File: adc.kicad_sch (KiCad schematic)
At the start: 0 parts

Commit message: Starting draft of ADC multiplexer
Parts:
- added D18: BAT54SW, Package_TO_SOT_SMD:SOT-323_SC-70, symbol Diode:BAT54SW
- added Q11, Q12: PMOS, symbol Simulation_SPICE:PMOS
- added Q13: 2N7002, Package_TO_SOT_SMD:SOT-323_SC-70, symbol Transistor_FET:2N7002
- added R40, R44: R, symbol Device:R
- added R45, R47: 1M, Resistor_SMD:R_0603_1608Metric, symbol Device:R
- added R46: 1k, Resistor_SMD:R_0603_1608Metric, symbol Device:R
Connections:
- new net: Q11.2 (G), Q12.2 (G), Q13.3 (D), R45.2
- new net: Q13.1 (G), R46.2, R47.1
- new net: Q11.1 (D), R40.1
- new net: Q11.3 (S), Q12.3 (S)
- new net +BATT: Q12.1 (D), R45.1
- new net GND: D18.1 (A), Q13.2 (S), R44.1, R47.2
- new net VBATT_ADC: D18.3 (COM), R40.2, R44.2
- new net VBATT_ADC_EN: R46.1
- new net VDD: D18.2 (K)
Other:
- note added: "Can multiplex any of the cell voltages to a single voltage divider and ADC pin This makes it possible to get a really good comparison as long as the ADC is linear"

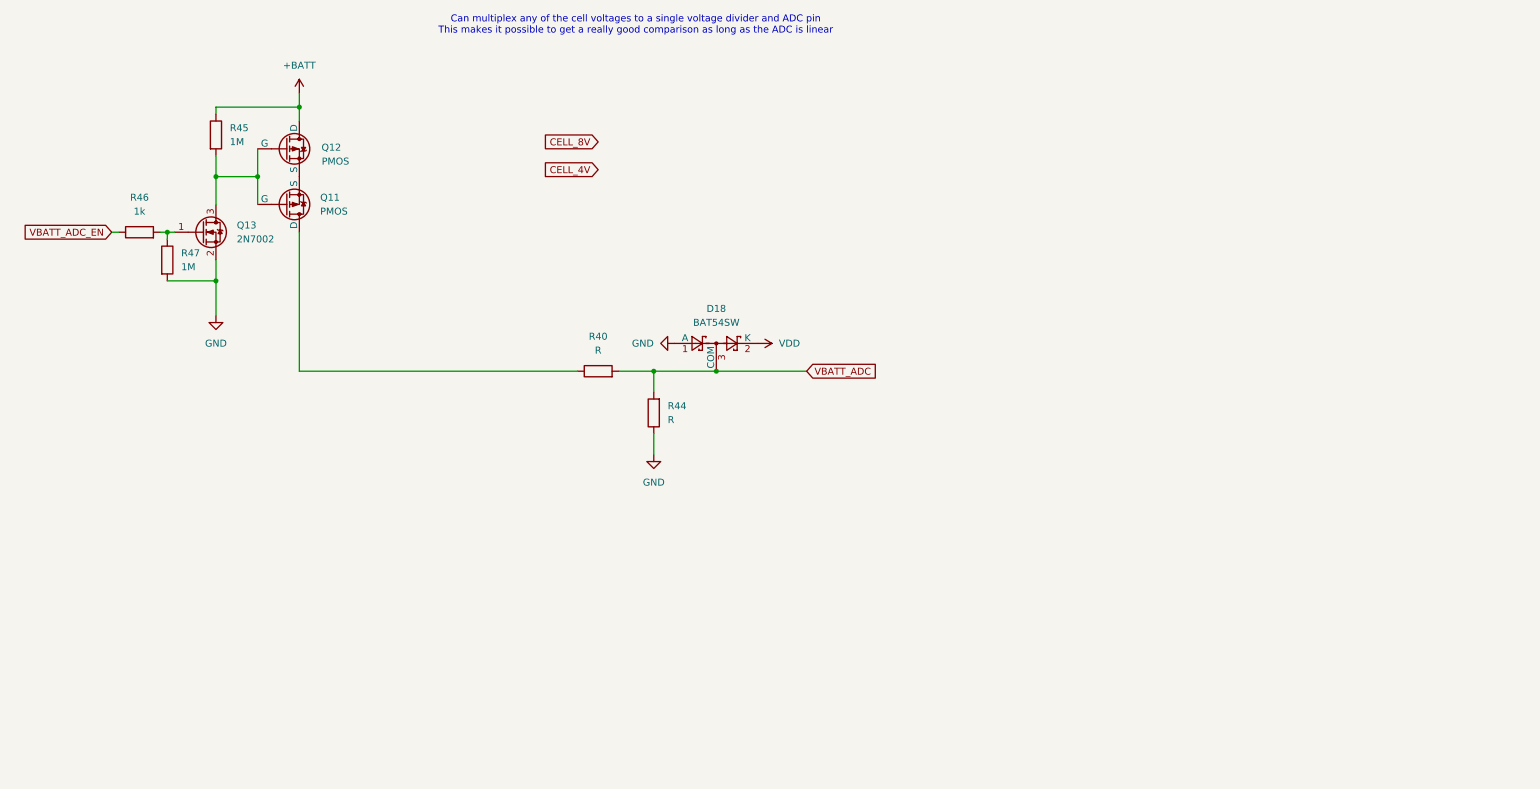
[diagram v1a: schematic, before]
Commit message: Adding ADC multiplexer, protection diodes
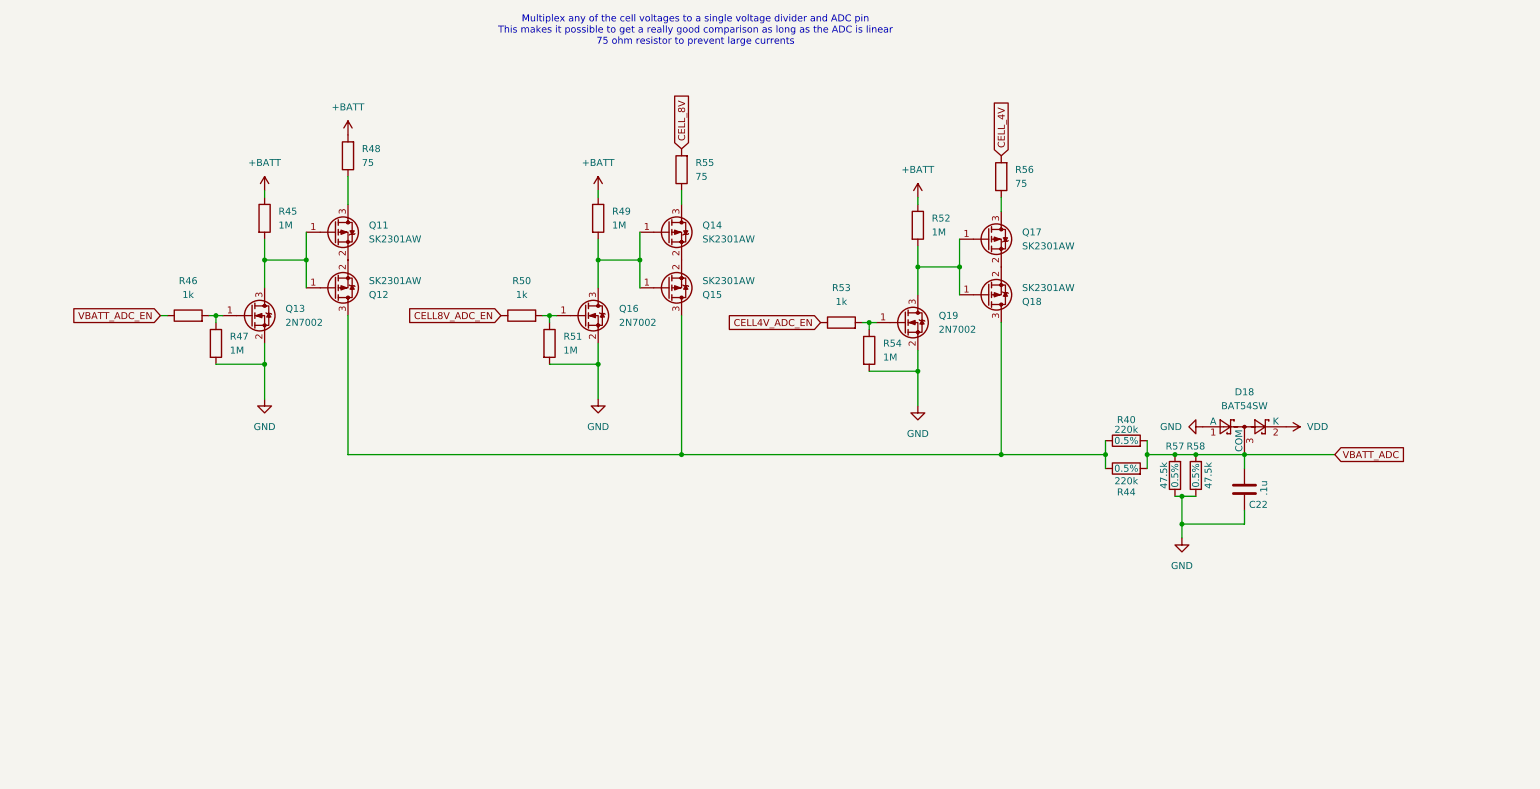
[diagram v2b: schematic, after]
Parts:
- removed Q11, Q12: PMOS, symbol Simulation_SPICE:PMOS
- added C22: .1u, Capacitor_SMD:C_0603_1608Metric, symbol Device:C
- added Q11, Q12, Q14, Q15, Q17, Q18: SK2301AW, Package_TO_SOT_SMD:SOT-323_SC-70, symbol JakeLib:SK2301AW
- added Q16, Q19: 2N7002, Package_TO_SOT_SMD:SOT-323_SC-70, symbol Transistor_FET:2N7002
- added R48, R55, R56: 75, Resistor_SMD:R_0603_1608Metric, symbol Device:R
- added R49, R51, R52, R54: 1M, Resistor_SMD:R_0603_1608Metric, symbol Device:R
- added R50, R53: 1k, Resistor_SMD:R_0603_1608Metric, symbol Device:R
- added R57, R58: 47.5k, Resistor_SMD:R_0402_1005Metric, symbol Device:R
- R40, R44: value R -> 220k; footprint (none) -> Resistor_SMD:R_0402_1005Metric; LCSC_Code (none) -> C851925; Tolerance (none) -> 0.5%
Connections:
- net +BATT: now also R48.2, R49.1, R52.1
- net CELL_4V: now also R56.2
- net CELL_8V: now also R55.2
- net GND: now also C22.2, Q16.2 (S), Q19.2 (S), R51.2, R54.2, R57.1, R58.1; no longer R44.1
- net VBATT_ADC: now also C22.1, R57.2, R58.2
- net at Q13.3 (D), R45.2: now also Q11.1 (G), Q12.1 (G)
- net at R40.1: now also R44.1, Q12.3 (D), Q15.3 (D), Q18.3 (D)
- new net: Q16.1 (G), R50.2, R51.1
- new net: Q11.2 (S), Q12.2 (S)
- new net: Q11.3 (D), R48.1
- new net: Q14.1 (G), Q15.1 (G), Q16.3 (D), R49.2
- new net: Q14.2 (S), Q15.2 (S)
- new net: Q14.3 (D), R55.1
- new net: Q17.1 (G), Q18.1 (G), Q19.3 (D), R52.2
- new net: Q17.3 (D), R56.1
- new net: Q17.2 (S), Q18.2 (S)
- new net: Q19.1 (G), R53.2, R54.1
- new net CELL4V_ADC_EN: R53.1
- new net CELL8V_ADC_EN: R50.1
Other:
- note added: "Multiplex any of the cell voltages to a single voltage divider and ADC pin This makes it possible to get a really good comparison as long as the ADC is linear 75 ohm resistor to prevent large currents"
- note removed: "Can multiplex any of the cell voltages to a single voltage divider and ADC pin This makes it possible to get a really good comparison as long as the ADC is linear"
- moved on the sheet: D18, Q13, R45, R46, R47

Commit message: Taking notes, doing some final adjustments to RC filter values
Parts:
- removed R40, R44: 220k, Resistor_SMD:R_0402_1005Metric, symbol Device:R
- removed R57, R58: 47.5k, Resistor_SMD:R_0402_1005Metric, symbol Device:R
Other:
- note added: "You want ~1/6 ratio so that 12V comes to around 2V. 1.5kohm max total impedance, because you are sampling frequently (Impedance goes to charge ~20pf adc capacitor, so that takes time, limiting sampling rate) (Also, at 80khz sampling rate, you have ~4uA current, to charge the 20pf capacitor, leading to voltage drop)"

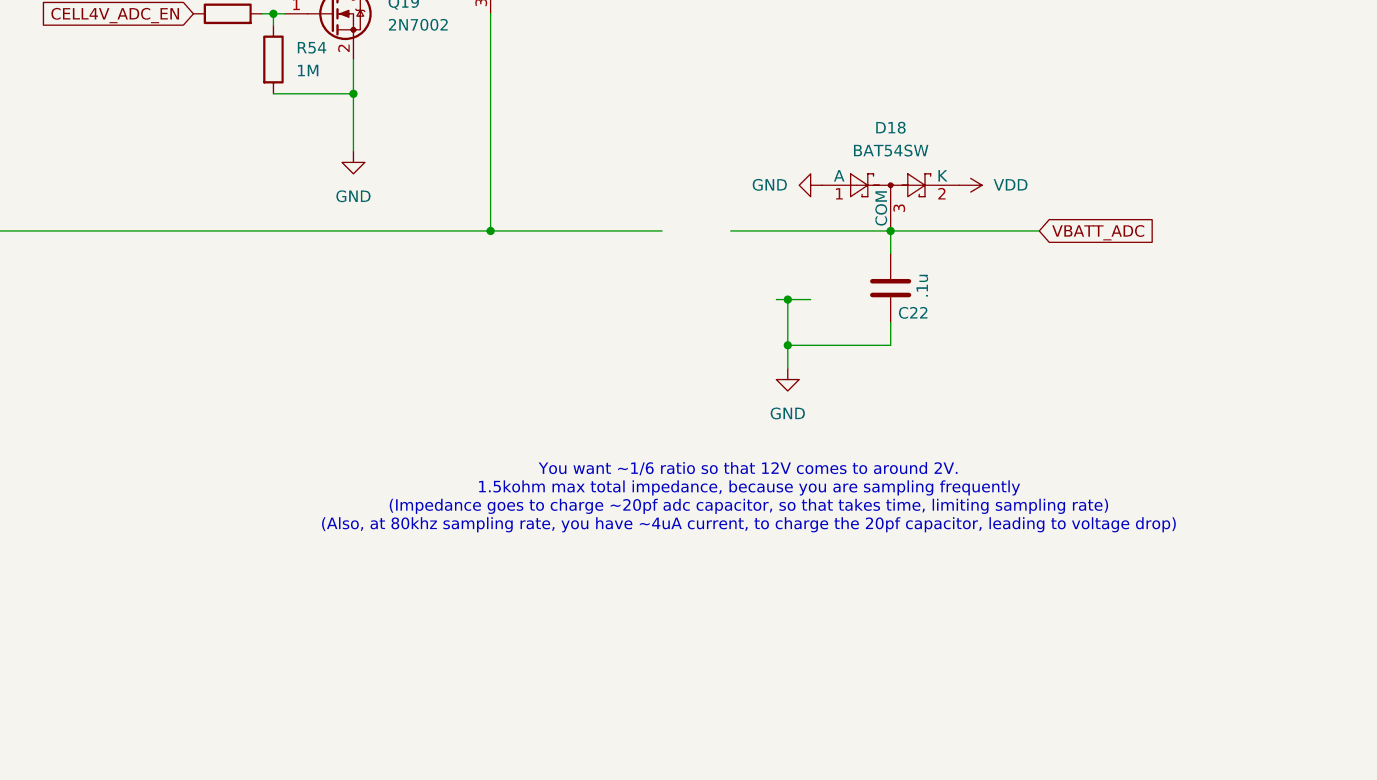
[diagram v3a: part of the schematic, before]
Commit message: L6388E mosfet drivers
Allow to enable/disable drivers
voltage dividers picked out
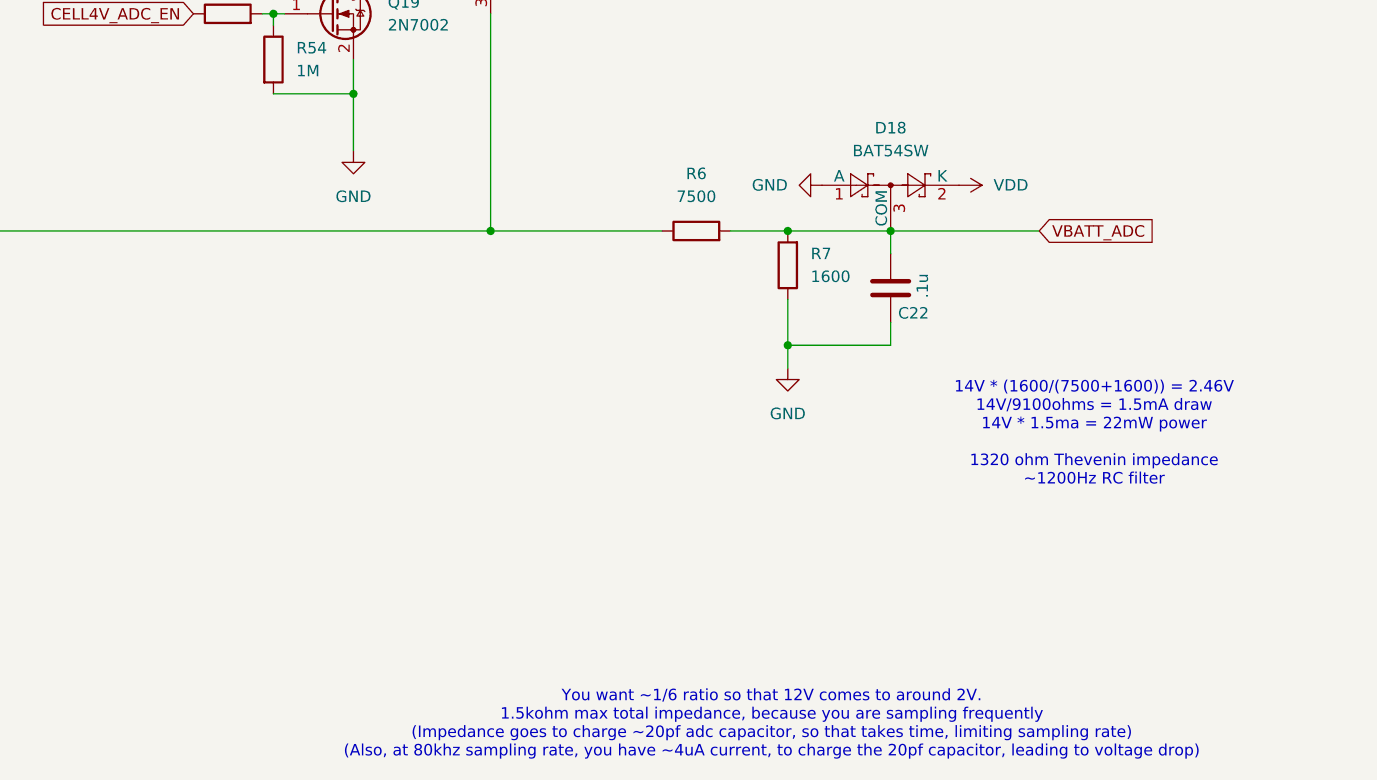
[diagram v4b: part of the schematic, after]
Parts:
- added R6: 7500, Resistor_SMD:R_0603_1608Metric, symbol Device:R
- added R7: 1600, symbol Device:R
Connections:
- net GND: now also R7.1
- net VBATT_ADC: now also R6.2, R7.2
- net at Q12.3 (D), Q15.3 (D), Q18.3 (D): now also R6.1
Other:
- note added: "14V * (1600/(7500+1600)) = 2.46V 14V/9100ohms = 1.5mA draw 14V * 1.5ma = 22mW power 1320 ohm Thevenin impedance ~1200Hz RC filter"
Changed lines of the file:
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@@
-	)
-	(junction
-		(at 224.79 105.41)
-		(diameter 0)
-		(color 0 0 0 0)
 	)
 	(junction
@@
 	)
 	(junction
+		(at 224.79 97.79)
+		(diameter 0)
+		(color 0 0 0 0)
+	)
+	(junction
 		(at 133.35 97.79)
 		(diameter 0)
@@
 	(wire
 		(pts
+			(xy 224.79 97.79) (xy 236.22 97.79)
+		)
+		(stroke
+			(width 0)
+			(type default)
+		)
+	)
+	(wire
+		(pts
 			(xy 110.49 72.39) (xy 109.22 72.39)
 		)
@@
 	(wire
 		(pts
-			(xy 218.44 97.79) (xy 236.22 97.79)
+			(xy 218.44 97.79) (xy 224.79 97.79)
 		)
 		(stroke
@@
 	(wire
 		(pts
-			(xy 224.79 105.41) (xy 227.33 105.41)
-		)
-		(stroke
-			(width 0)
-			(type default)
-		)
-	)
-	(wire
-		(pts
 			(xy 167.64 82.55) (xy 176.53 82.55)
 		)
@@
 		(pts
 			(xy 184.15 63.5) (xy 184.15 68.58)
-		)
-		(stroke
-			(width 0)
-			(type default)
-		)
-	)
-	(wire
-		(pts
-			(xy 223.52 105.41) (xy 224.79 105.41)
 		)
 		(stroke
@@
 	(text "You want ~1/6 ratio so that 12V comes to around 2V.\n1.5kohm max total impedance, because you are sampling frequently\n(Impedance goes to charge ~20pf adc capacitor, so that takes time, limiting sampling rate)\n(Also, at 80khz sampling rate, you have ~4uA current, to charge the 20pf capacitor, leading to voltage drop)"
 		(exclude_from_sim no)
-		(at 220.472 127.508 0)
+		(at 223.012 152.654 0)
+		(effects
+			(font
+				(size 1.27 1.27)
+			)
+		)
+	)
+	(text "14V * (1600/(7500+1600)) = 2.46V\n14V/9100ohms = 1.5mA draw\n14V * 1.5ma = 22mW power\n\n1320 ohm Thevenin impedance\n~1200Hz RC filter"
+		(exclude_from_sim no)
+		(at 258.826 120.396 0)
 		(effects
 			(font
@@
 	(symbol
 		(lib_id "Device:R")
+		(at 214.63 97.79 90)
+		(unit 1)
+		(exclude_from_sim no)
+		(in_bom yes)
+		(on_board yes)
+		(dnp no)
+		(fields_autoplaced yes)
+		(property "Reference" "R6"
+			(at 214.63 91.44 90)
+			(effects
+				(font
+					(size 1.27 1.27)
+				)
+			)
+		)
+		(property "Value" "7500"
+			(at 214.63 93.98 90)
+			(effects
+				(font
+					(size 1.27 1.27)
+				)
+			)
+		)
+		(property "Footprint" "Resistor_SMD:R_0603_1608Metric"
+			(at 214.63 99.568 90)
+			(effects
+				(font
+					(size 1.27 1.27)
+				)
+				(hide yes)
+			)
+		)
+		(property "Datasheet" "~"
+			(at 214.63 97.79 0)
+			(effects
+				(font
+					(size 1.27 1.27)
+				)
+				(hide yes)
+			)
+		)
+		(property "Description" "Resistor"
+			(at 214.63 97.79 0)
+			(effects
+				(font
+					(size 1.27 1.27)
+				)
+				(hide yes)
+			)
+		)
+		(pin "2"
+		)
+		(pin "1"
+		)
+		(instances
+			(project "JPBms2"
+				(path "/d86e471c-a8be-422d-a5d1-5a4699b7b766/4f52082d-cd8b-4070-bfed-876b38f927ef"
+					(reference "R6")
+					(unit 1)
+				)
+			)
+		)
+	)
+	(symbol
+		(lib_id "Device:R")
 		(at 43.18 72.39 90)
 		(unit 1)
@@
 					(unit 1)
 				)
+			)
+		)
+	)
+	(symbol
+		(lib_id "Device:R")
+		(at 224.79 101.6 180)
+		(unit 1)
+		(exclude_from_sim no)
+		(in_bom yes)
+		(on_board yes)
+		(dnp no)
+		(fields_autoplaced yes)
+		(property "Reference" "R7"
+			(at 227.33 100.3299 0)
+			(effects
+				(font
+					(size 1.27 1.27)
+				)
+				(justify right)
+			)
+		)
+		(property "Value" "1600"
+			(at 227.33 102.8699 0)
+			(effects
+				(font
+					(size 1.27 1.27)
+				)
+				(justify right)
+			)
+		)
+		(property "Footprint" ""
+			(at 226.568 101.6 90)
+			(effects
+				(font
+					(size 1.27 1.27)
+				)
+				(hide yes)
+			)
+		)
+		(property "Datasheet" "~"
+			(at 224.79 101.6 0)
+			(effects
+				(font
+					(size 1.27 1.27)
+				)
+				(hide yes)
+			)
+		)
+		(property "Description" "Resistor"
+			(at 224.79 101.6 0)
+			(effects
+				(font
+					(size 1.27 1.27)
+				)
+				(hide yes)
+			)
+		)
+		(pin "1"
+		)
+		(pin "2"
+		)
+		(instances
+			(project "JPBms2"
+				(path "/d86e471c-a8be-422d-a5d1-5a4699b7b766/4f52082d-cd8b-4070-bfed-876b38f927ef"
+					(reference "R7")
+					(unit 1)
+				)

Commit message: New schematic done
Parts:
- R7: footprint (none) -> Resistor_SMD:R_0603_1608Metric

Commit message: A couple of part selections
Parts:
- Q11, Q12, Q14, Q15, Q17, Q18: LCSC_Code (none) -> C962722
- R6: LCSC_Code (none) -> C23234
- R7: LCSC_Code (none) -> C22847
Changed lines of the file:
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@@
 			)
 		)
-		(property "Datasheet" "http://www.vishay.com/docs/70209/70209.pdf"
+		(property "Datasheet" "https://www.lcsc.com/datasheet/lcsc_datasheet_2311241453_Shikues-SK2301AW_C962722.pdf"
 			(at 74.93 60.96 0)
 			(effects
@@
 		)
 		(property "Tolerance" ""
+			(at 69.85 57.15 0)
+			(effects
+				(font
+					(size 1.27 1.27)
+				)
+				(hide yes)
+			)
+		)
+		(property "LCSC_Code" "C962722"
 			(at 69.85 57.15 0)
 			(effects
@@
 			)
 		)
+		(property "LCSC_Code" "C23234"
+			(at 214.63 97.79 0)
+			(effects
+				(font
+					(size 1.27 1.27)
+				)
+				(hide yes)
+			)
+		)
 		(pin "2"
 		)
@@
 			)
 		)
-		(property "Datasheet" "http://www.vishay.com/docs/70209/70209.pdf"
+		(property "Datasheet" "https://www.lcsc.com/datasheet/lcsc_datasheet_2311241453_Shikues-SK2301AW_C962722.pdf"
 			(at 74.93 63.5 0)
 			(effects
@@
 		)
 		(property "Tolerance" ""
+			(at 69.85 67.31 0)
+			(effects
+				(font
+					(size 1.27 1.27)
+				)
+				(hide yes)
+			)
+		)
+		(property "LCSC_Code" "C962722"
 			(at 69.85 67.31 0)
 			(effects
@@
 			)
 		)
+		(property "LCSC_Code" "C22847"
+			(at 224.79 101.6 0)
+			(effects
+				(font
+					(size 1.27 1.27)
+				)
+				(hide yes)
+			)
+		)
 		(pin "1"
 		)
@@
 			)
 		)
-		(property "Datasheet" "http://www.vishay.com/docs/70209/70209.pdf"
+		(property "Datasheet" "https://www.lcsc.com/datasheet/lcsc_datasheet_2311241453_Shikues-SK2301AW_C962722.pdf"
 			(at 135.89 63.5 0)
 			(effects
@@
 		)
 		(property "Tolerance" ""
+			(at 130.81 67.31 0)
+			(effects
+				(font
+					(size 1.27 1.27)
+				)
+				(hide yes)
+			)
+		)
+		(property "LCSC_Code" "C962722"
 			(at 130.81 67.31 0)
 			(effects
@@
 			)
 		)
-		(property "Datasheet" "http://www.vishay.com/docs/70209/70209.pdf"
+		(property "Datasheet" "https://www.lcsc.com/datasheet/lcsc_datasheet_2311241453_Shikues-SK2301AW_C962722.pdf"
 			(at 135.89 60.96 0)
 			(effects
@@
 		)
 		(property "Tolerance" ""
+			(at 130.81 57.15 0)
+			(effects
+				(font
+					(size 1.27 1.27)
+				)
+				(hide yes)
+			)
+		)
+		(property "LCSC_Code" "C962722"
 			(at 130.81 57.15 0)
 			(effects
@@
 			)
 		)
-		(property "Datasheet" "http://www.vishay.com/docs/70209/70209.pdf"
+		(property "Datasheet" "https://www.lcsc.com/datasheet/lcsc_datasheet_2311241453_Shikues-SK2301AW_C962722.pdf"
 			(at 194.31 62.23 0)
 			(effects
@@
 		)
 		(property "Tolerance" ""
+			(at 189.23 58.42 0)
+			(effects
+				(font
+					(size 1.27 1.27)
+				)
+				(hide yes)
+			)
+		)
+		(property "LCSC_Code" "C962722"
 			(at 189.23 58.42 0)
 			(effects
@@
 			)
 		)
-		(property "Datasheet" "http://www.vishay.com/docs/70209/70209.pdf"
+		(property "Datasheet" "https://www.lcsc.com/datasheet/lcsc_datasheet_2311241453_Shikues-SK2301AW_C962722.pdf"
 			(at 194.31 64.77 0)
 			(effects
@@
 			(at 189.23 68.58 0)
 			(effects
+				(font
+					(size 1.27 1.27)
+				)
+				(hide yes)
+			)
+		)
+		(property "LCSC_Code" "C962722"
+			(at 189.23 68.58 0)
+			(effects

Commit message: Decent pass
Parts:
- added R43, R48, R53: 1M, Resistor_SMD:R_0603_1608Metric, symbol Device:R
- renumbered C22 to C20, D18 to D16, Q11 to Q14, Q12 to Q15, Q14 to Q17, Q15 to Q18, Q17 to Q20, Q18 to Q21, R46 to R40, R47 to R41, R45 to R42, R48 to R44, R50 to R45, R51 to R46, R49 to R47, R55 to R49, R53 to R50, R54 to R51, R56 to R54, R6 to R55, R7 to R56
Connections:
- net at Q13.3 (D), Q14.1 (G), Q15.1 (G)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: now also R43.1
- net at Q14.2 (S), Q15.2 (S): now also R43.2
- net at Q16.3 (D), Q17.1 (G), Q18.1 (G)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: now also R48.1
- net at Q17.2 (S), Q18.2 (S): now also R48.2
- net at Q19.3 (D), Q20.1 (G), Q21.1 (G)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: now also R53.1
- net at Q20.2 (S), Q21.2 (S): now also R53.2

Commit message: Routing pt1
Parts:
- renumbered C20 to C22, D16 to D18, Q14 to Q11, Q15 to Q12, Q17 to Q14, Q18 to Q15, Q20 to Q17, Q21 to Q18, R43 to R38, R48 to R40, R53 to R44, R42 to R45, R40 to R46, R41 to R47, R44 to R48, R47 to R49, R45 to R50, R46 to R51, R50 to R53, R51 to R54, R49 to R55, R54 to R56, R55 to R6, R56 to R7
